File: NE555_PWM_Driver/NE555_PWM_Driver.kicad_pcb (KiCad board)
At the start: 2 copper layers, 45 x 59 mm, 13 parts, among them J1 Input, J2 Output, Q1 IRFZ44N, U1 NE555P

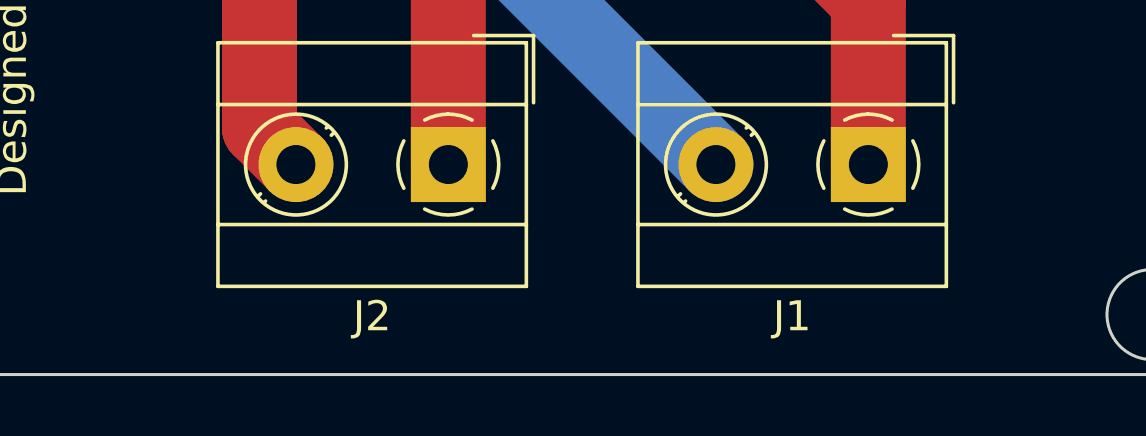
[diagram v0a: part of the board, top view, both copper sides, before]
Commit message: added i/o polarity on silkscreen
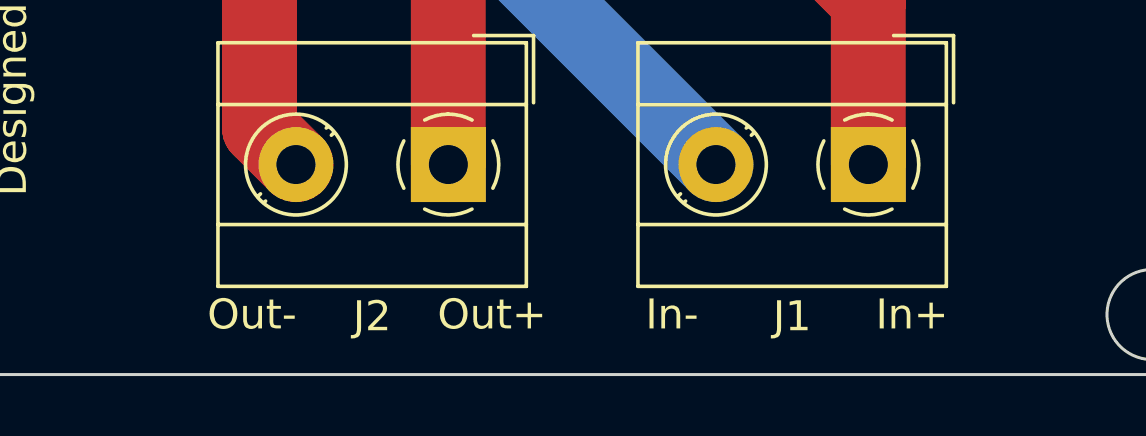
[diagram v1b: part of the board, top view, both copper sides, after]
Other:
- board text added: "In+"
- board text added: "In-"
- board text added: "Out+"
- board text added: "Out-"
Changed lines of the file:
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@@
+    (effects (font (size 1 1) (thickness 0.15)))
+  )
+  (gr_text "Out+\n" (at 174 125) (layer "F.SilkS")
+    (effects (font (size 1 1) (thickness 0.15)))
+  )
+  (gr_text "In-\n" (at 180 125) (layer "F.SilkS")
     (effects (font (size 1 1) (thickness 0.15)))
   )
@@
     (effects (font (size 1 1) (thickness 0.15)))
   )
+  (gr_text "Out-\n" (at 166 125) (layer "F.SilkS")
+    (effects (font (size 1 1) (thickness 0.15)))
+  )
   (gr_text "RED\n" (at 196 84.5 90) (layer "F.SilkS")
     (effects (font (size 1 1) (thickness 0.15)))
   )
+  (gr_text "In+\n" (at 188 125) (layer "F.SilkS")
+    (effects (font (size 1 1) (thickness 0.15)))
+  )
